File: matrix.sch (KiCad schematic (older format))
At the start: 285 parts, among them SW2 SW_SPDT, SW3 SW_SPDT

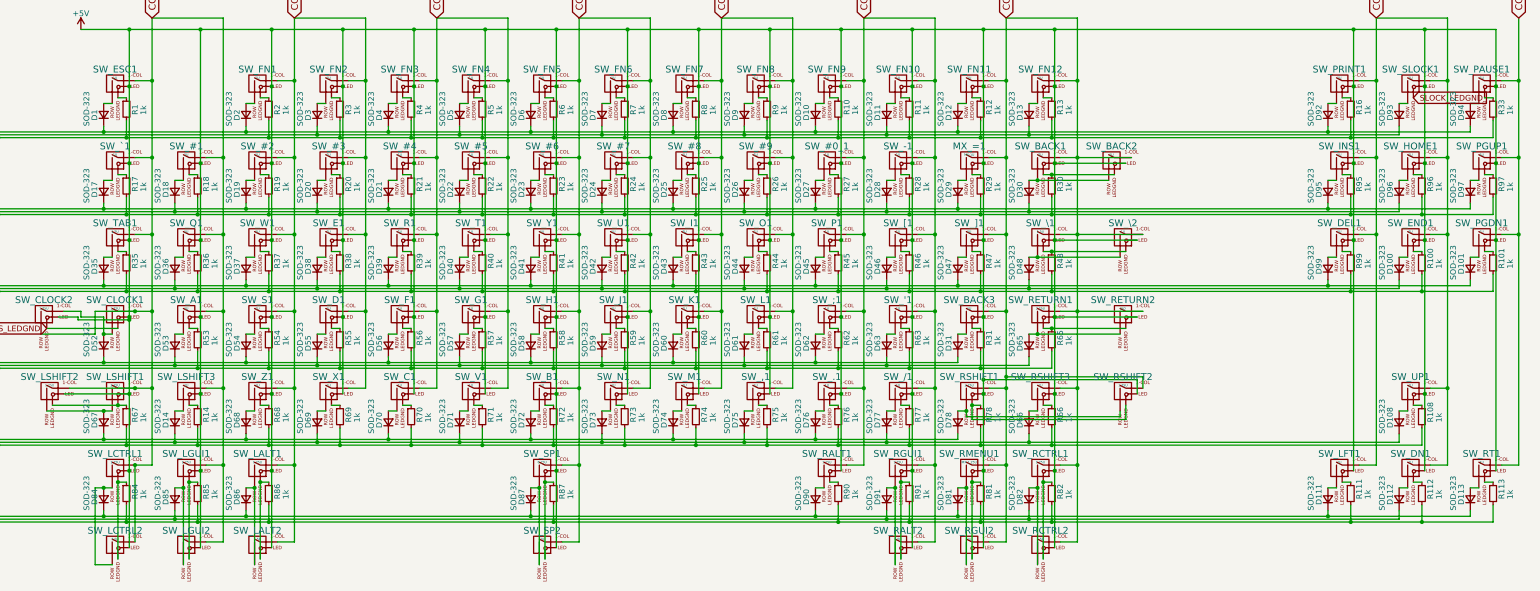
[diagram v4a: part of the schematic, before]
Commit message: BOM and POS file updates
Working on updating the positioning and BOM files for use with JLCPCB.
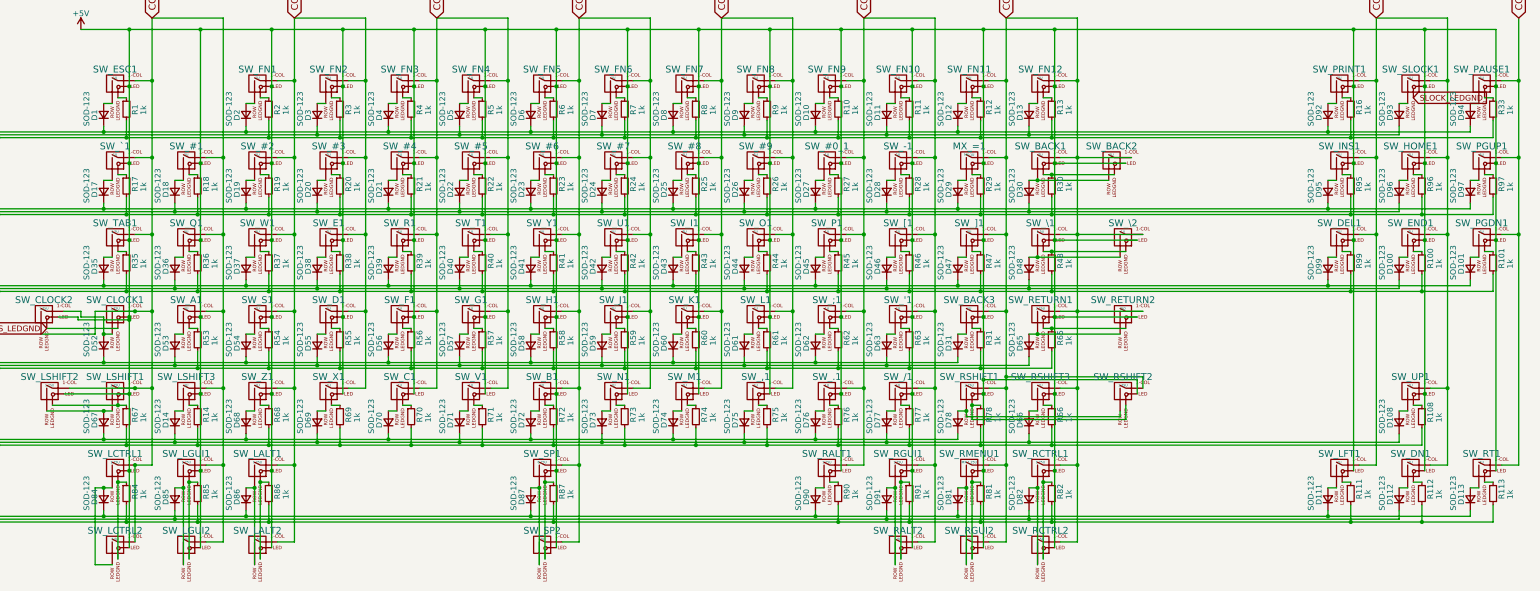
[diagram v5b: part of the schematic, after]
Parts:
- D1, D10, D100, D101, D108, D11, D111, D112, D113, D12, D13, D14, D17, D18, D19, D2, D20, D21, D22, D23, D24, D25, D26, D27, D28, D29, D3, D30, D31, D35, D36, D37, D38, D39, D4, D40, D41, D42, D43, D44, D45, D46, D47, D48, D5, D52, D53, D54, D55, D56, D57, D58, D59, D6, D60, D61, D62, D63, D65, D66, D67, D68, D69, D7, D70, D71, D72, D73, D74, D75, D76, D77, D78, D8, D81, D82, D84, D85, D86, D87, D9, D90, D91, D92, D93, D94, D95, D96, D97, D99: value SOD-323 -> SOD-123

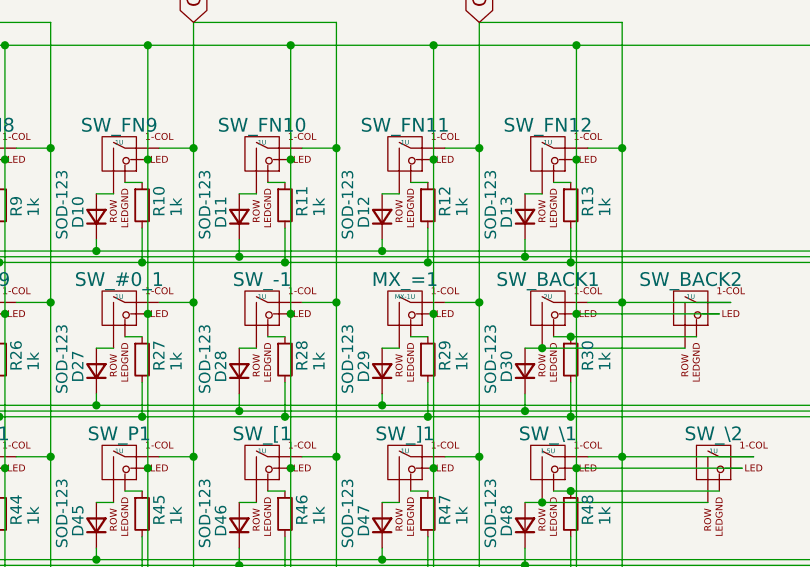
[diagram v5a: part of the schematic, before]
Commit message: Fix PCB footprint mistake
There was a mistake with one of the footprints, which was not changed. All footprints are now Alps-compatible and the Gerber files have been updated.
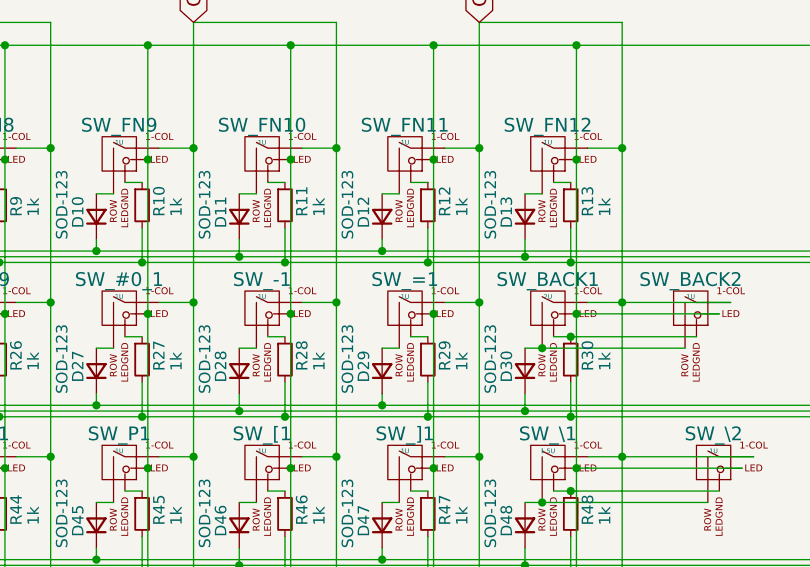
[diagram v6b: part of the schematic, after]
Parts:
- SW_=1: renamed from MX_=1; value MX-1U -> 1U; footprint MX_Alps_Hybrid:MXOnly-1U -> MX_Alps_Hybrid:MX-1U
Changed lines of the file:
@@
 $EndComp
 $Comp
-L MX_Alps_Hybrids:MX-1U MX_=1
+L MX_Alps_Hybrids:MX-1U SW_=1
 U 1 1 5A2E409A
 P 12325 3425
-F 0 "MX_=1" H 12325 3550 60  0000 C CNN
-F 1 "MX-1U" H 12325 3475 20  0000 C CNN
-F 2 "MX_Alps_Hybrid:MXOnly-1U" H 12300 3400 60  0001 C CNN
+F 0 "SW_=1" H 12325 3550 60  0000 C CNN
+F 1 "1U" H 12325 3475 20  0000 C CNN
+F 2 "MX_Alps_Hybrid:MX-1U" H 12300 3400 60  0001 C CNN
 F 3 "" H 12300 3400 60  0001 C CNN
 	1    12325 3425

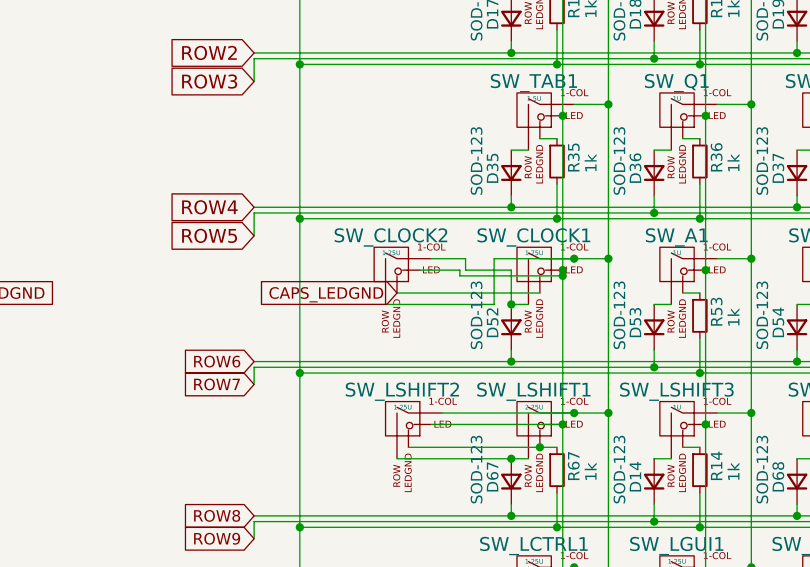
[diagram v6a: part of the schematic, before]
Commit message: Updated for 3800 style Capslock
Added additional footprint for the 3800-style caps lock key. Gerbers updated as well.
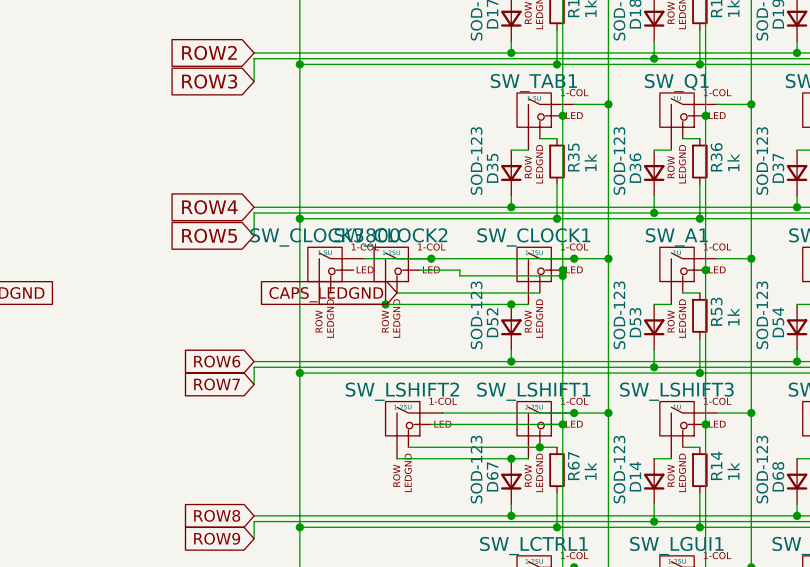
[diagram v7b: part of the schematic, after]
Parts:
- added SW_CLOCK3800: 1.5U, MX_Alps_Hybrid:ALPS-1.5U, symbol MX_Alps_Hybrids:MX-1.5U
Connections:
- net COL0: now also SW_CLOCK2.1 (COL), SW_CLOCK3800.1 (COL); no longer SW_CLOCK2.2 (ROW)
- net at D52.2 (A), SW_CLOCK1.2 (ROW): now also SW_CLOCK2.2 (ROW), SW_CLOCK3800.2 (ROW); no longer SW_CLOCK2.1 (COL)
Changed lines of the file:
@@
 	12925 4275 12850 4275
 Wire Wire Line
-	4225 4900 4850 4900
-Wire Wire Line
 	4800 4950 4725 4950
 Wire Wire Line
@@
 Wire Wire Line
 	12850 4950 12925 4950
-Connection ~ 5000 4750
 Connection ~ 4950 3450
 Connection ~ 4950 4125
@@
 	4925 6600 4925 6450
 Wire Wire Line
-	4650 4750 5000 4750
-Wire Wire Line
-	4650 4750 4650 4950
-Wire Wire Line
-	4650 4950 4175 4950
-Wire Wire Line
-	4725 4950 4725 4800
-Wire Wire Line
-	4725 4800 4525 4800
-Wire Wire Line
-	4525 4800 4525 4750
-Wire Wire Line
-	4525 4750 4375 4750
-Wire Wire Line
-	4325 4800 4500 4800
-Wire Wire Line
 	4500 4800 4500 4825
 Wire Wire Line
@@
 Connection ~ 4925 6600
 Connection ~ 3800 5925
-Connection ~ 4725 4950
 Connection ~ 4850 6250
 Wire Wire Line
@@
 	12850 6575 16100 6575
 Connection ~ 12850 6575
+Wire Wire Line
+	4225 4900 4850 4900
+Wire Wire Line
+	4085 4750 4375 4750
+Wire Wire Line
+	4325 4800 4500 4800
+Wire Wire Line
+	4375 4750 5000 4750
+Connection ~ 4375 4750
+Connection ~ 5000 4750
+$Comp
+L MX_Alps_Hybrids:MX-1.5U SW_CLOCK3800
+U 1 1 62434DCA
+P 3910 4775
+F 0 "SW_CLOCK3800" H 3910 4900 60  0000 C CNN
+F 1 "1.5U" H 3910 4825 20  0000 C CNN
+F 2 "MX_Alps_Hybrid:ALPS-1.5U" H 3885 4750 60  0001 C CNN
+F 3 "" H 3885 4750 60  0001 C CNN
+	1    3910 4775
+	1    0    0    -1
+$EndComp
+Wire Wire Line
+	3885 4950 4175 4950
+Wire Wire Line
+	4175 4950 4725 4950
+Connection ~ 4175 4950
+Connection ~ 4725 4950
 $EndSCHEMATC
